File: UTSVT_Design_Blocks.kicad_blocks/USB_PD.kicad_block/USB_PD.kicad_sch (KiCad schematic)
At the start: 30 parts, among them IC1 CYPD3177-24LQXQ, Q1 SI7997DP-T1-GE3, Q3 SI7997DP-T1-GE3

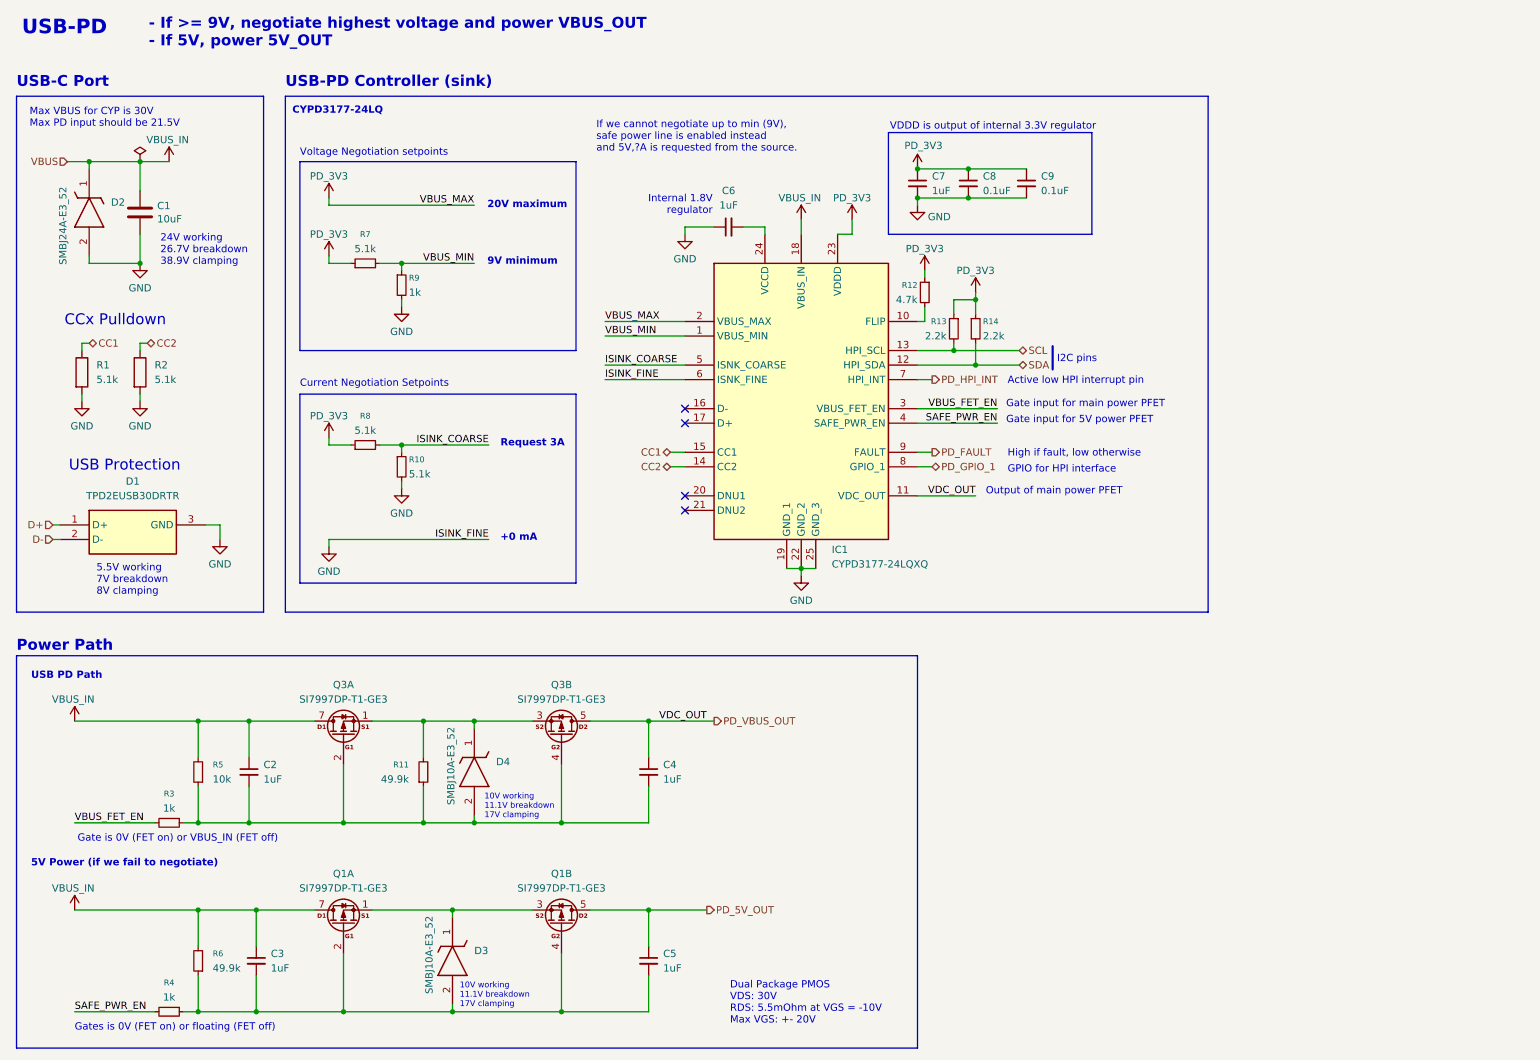
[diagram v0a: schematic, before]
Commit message: added testpoints and LED to design block
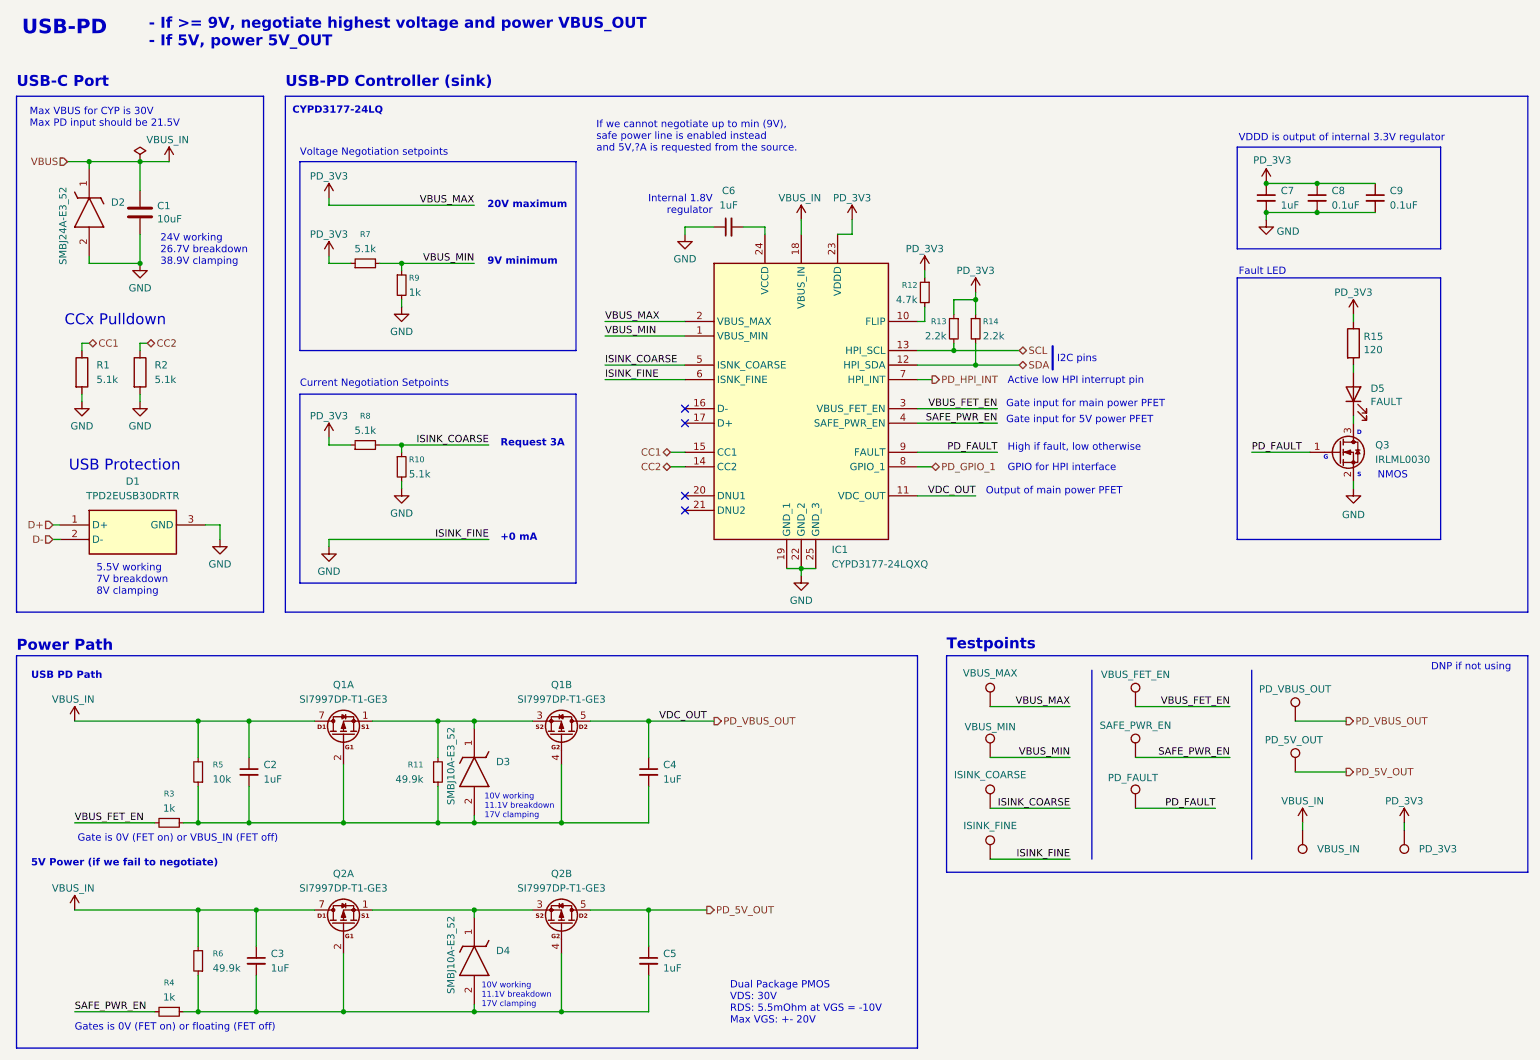
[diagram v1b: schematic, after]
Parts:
- added D5: FAULT, LED_SMD:LED_0603_1608Metric_Pad1.05x0.95mm_HandSolder, symbol Device:LED
- added Q3: IRLML0030, Package_TO_SOT_SMD:SOT-23, symbol Transistor_FET:IRLML0030
- added R15: 120, Resistor_SMD:R_0603_1608Metric_Pad0.98x0.95mm_HandSolder, symbol Device:R
- added TP1: VBUS_MAX, TestPoint:TestPoint_Pad_1.0x1.0mm, symbol Connector:TestPoint
- added TP10: VBUS_IN, TestPoint:TestPoint_Pad_1.0x1.0mm, symbol Connector:TestPoint
- added TP11: PD_3V3, TestPoint:TestPoint_Pad_1.0x1.0mm, symbol Connector:TestPoint
- added TP2: VBUS_MIN, TestPoint:TestPoint_Pad_1.0x1.0mm, symbol Connector:TestPoint
- added TP3: ISINK_COARSE, TestPoint:TestPoint_Pad_1.0x1.0mm, symbol Connector:TestPoint
- added TP4: ISINK_FINE, TestPoint:TestPoint_Pad_1.0x1.0mm, symbol Connector:TestPoint
- added TP5: VBUS_FET_EN, TestPoint:TestPoint_Pad_1.0x1.0mm, symbol Connector:TestPoint
- added TP6: SAFE_PWR_EN, TestPoint:TestPoint_Pad_1.0x1.0mm, symbol Connector:TestPoint
- added TP7: PD_FAULT, TestPoint:TestPoint_Pad_1.0x1.0mm, symbol Connector:TestPoint
- added TP8: PD_VBUS_OUT, TestPoint:TestPoint_Pad_1.0x1.0mm, symbol Connector:TestPoint
- added TP9: PD_5V_OUT, TestPoint:TestPoint_Pad_1.0x1.0mm, symbol Connector:TestPoint
- renumbered D4 to D3, D3 to D4, Q3 to Q1, Q1 to Q2
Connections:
- net GND: now also Q3.2 (S), TP4.1
- net ISINK_COARSE: now also TP3.1
- net PD_3V3: now also R15.1, TP1.1, TP11.1
- net PD_5V_OUT: now also TP9.1
- net PD_FAULT: now also Q3.1 (G), TP7.1
- net PD_VBUS_OUT: now also TP8.1
- net SAFE_PWR_EN: now also TP6.1
- net VBUS_FET_EN: now also TP5.1
- net VBUS_IN: now also TP10.1
- net VBUS_MIN: now also TP2.1
- new net: D5.1 (K), Q3.3 (D)
- new net: D5.2 (A), R15.2
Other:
- note added: "D"
- note added: "DNP if not using"
- note added: "Fault LED"
- note added: "G"
- note added: "NMOS"
- note added: "S"
- note added: "Testpoints"
- moved on the sheet: C7, C8, C9, D4, R11

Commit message: updates
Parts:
- D5: Color (none) -> Red; LCSC P/N C67272 -> C84263; Mfg XL-1608UBC-06A -> NCD0603R1; P/N XL-1608UBC-06A -> NCD0603R1
- TP10, TP11, TP8, TP9: footprint TestPoint:TestPoint_Pad_1.0x1.0mm -> Connector_PinHeader_2.54mm:PinHeader_1x01_P2.54mm_Vertical
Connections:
- net GND renamed PD_GND
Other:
- note added: "Fault LED: on if PD faults (failed negotiation or overvoltage protection fault)"
- note added: "If VBUS_IN >= 9V, negotiate highest voltage and power VBUS_OUT Else, negotiate for 5V and power 5V_OUT"
- note removed: "- If >= 9V, negotiate highest voltage and power VBUS_OUT - If 5V, power 5V_OUT"
- note removed: "Fault LED"
- moved on the sheet: C7, C8, C9, D1, Q3, R1, R15, R2
